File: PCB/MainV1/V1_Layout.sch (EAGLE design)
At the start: 50 parts, among them IC1 AD826N, IC3 AD623R, U2 MB85RC256VPF-G-JNERE2, X1 STEREOJACK

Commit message: Review changes complete. Starting layout
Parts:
- removed D7, D8: 1N4004, diode:1N4004
- C10: value (none) -> 10uF
- C11, C9: value (none) -> 1uF
- C7: value 1uF -> 10nF
- C8: value (none) -> 100nF
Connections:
- net AGND: no longer D7.C, D8.A
- net D6: no longer U2.A2
- net D7: no longer U2.A1
- net D8: no longer U2.A0
- net GND: now also U2.A0, U2.A1, U2.A2; no longer D7.A, D8.C
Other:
- note added: "Address: 0x1D and 0x1C"
- note added: "Address: 0x50"
- note added: "Address: 0x90"
- note removed: "Address changable from Arduino"
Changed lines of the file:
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@@
 <part name="SUPPLY15" library="supply2" library_urn="urn:adsk.eagle:library:372" deviceset="GND" device=""/>
 <part name="+3V10" library="supply1" library_urn="urn:adsk.eagle:library:371" deviceset="+3V3" device=""/>
-<part name="D7" library="diode" library_urn="urn:adsk.eagle:library:210" deviceset="1N4004" device="" package3d_urn="urn:adsk.eagle:package:43336/1"/>
-<part name="D8" library="diode" library_urn="urn:adsk.eagle:library:210" deviceset="1N4004" device="" package3d_urn="urn:adsk.eagle:package:43336/1"/>
-<part name="SUPPLY16" library="supply2" library_urn="urn:adsk.eagle:library:372" deviceset="GND" device=""/>
-<part name="AGND3" library="supply1" library_urn="urn:adsk.eagle:library:371" deviceset="AGND" device=""/>
 <part name="PWR" library="pinhead" library_urn="urn:adsk.eagle:library:325" deviceset="PINHD-1X2" device="" package3d_urn="urn:adsk.eagle:package:22435/2"/>
 <part name="R9" library="rcl" library_urn="urn:adsk.eagle:library:334" deviceset="R-US_" device="R0603" package3d_urn="urn:adsk.eagle:package:23555/2" value="10k"/>
@@
 <part name="SUPPLY20" library="supply2" library_urn="urn:adsk.eagle:library:372" deviceset="GND" device=""/>
 <part name="C6" library="rcl" library_urn="urn:adsk.eagle:library:334" deviceset="C-EU" device="C0603" package3d_urn="urn:adsk.eagle:package:23616/2" value="100nF"/>
-<part name="C7" library="rcl" library_urn="urn:adsk.eagle:library:334" deviceset="C-EU" device="C0603" package3d_urn="urn:adsk.eagle:package:23616/2" value="1uF"/>
-<part name="C8" library="rcl" library_urn="urn:adsk.eagle:library:334" deviceset="C-EU" device="025-030X050" package3d_urn="urn:adsk.eagle:package:23631/1"/>
-<part name="C9" library="rcl" library_urn="urn:adsk.eagle:library:334" deviceset="C-EU" device="025-030X050" package3d_urn="urn:adsk.eagle:package:23631/1"/>
-<part name="C10" library="rcl" library_urn="urn:adsk.eagle:library:334" deviceset="CPOL-EU" device="E3.5-8" package3d_urn="urn:adsk.eagle:package:23360/2"/>
-<part name="C11" library="rcl" library_urn="urn:adsk.eagle:library:334" deviceset="C-EU" device="025-030X050" package3d_urn="urn:adsk.eagle:package:23631/1"/>
+<part name="C7" library="rcl" library_urn="urn:adsk.eagle:library:334" deviceset="C-EU" device="C0603" package3d_urn="urn:adsk.eagle:package:23616/2" value="10nF"/>
+<part name="C8" library="rcl" library_urn="urn:adsk.eagle:library:334" deviceset="C-EU" device="025-030X050" package3d_urn="urn:adsk.eagle:package:23631/1" value="100nF"/>
+<part name="C9" library="rcl" library_urn="urn:adsk.eagle:library:334" deviceset="C-EU" device="025-030X050" package3d_urn="urn:adsk.eagle:package:23631/1" value="1uF"/>
+<part name="C10" library="rcl" library_urn="urn:adsk.eagle:library:334" deviceset="CPOL-EU" device="E3.5-8" package3d_urn="urn:adsk.eagle:package:23360/2" value="10uF"/>
+<part name="C11" library="rcl" library_urn="urn:adsk.eagle:library:334" deviceset="C-EU" device="025-030X050" package3d_urn="urn:adsk.eagle:package:23631/1" value="1uF"/>
 <part name="SUPPLY21" library="supply2" library_urn="urn:adsk.eagle:library:372" deviceset="GND" device=""/>
 <part name="+3V13" library="supply1" library_urn="urn:adsk.eagle:library:371" deviceset="+3V3" device=""/>
 <part name="SUPPLY22" library="supply2" library_urn="urn:adsk.eagle:library:372" deviceset="GND" device=""/>
+<part name="SUPPLY24" library="supply2" library_urn="urn:adsk.eagle:library:372" deviceset="GND" device=""/>
+<part name="AGND3" library="supply1" library_urn="urn:adsk.eagle:library:371" deviceset="AGND" device=""/>
 </parts>
 <sheets>
@@
 <wire x1="342.9" y1="55.88" x2="342.9" y2="116.84" width="0.254" layer="94"/>
 <text x="228.6" y="111.76" size="2.54" layer="94">EGC Signal Aplification</text>
-<text x="43.18" y="111.76" size="1.778" layer="97">Address changable from Arduino</text>
+<text x="43.18" y="111.76" size="1.778" layer="97">Address: 0x50</text>
 <wire x1="17.78" y1="55.88" x2="17.78" y2="-2.54" width="0.254" layer="94"/>
 <wire x1="17.78" y1="-2.54" x2="88.9" y2="-2.54" width="0.254" layer="94"/>
@@
 <wire x1="167.64" y1="-2.54" x2="88.9" y2="-2.54" width="0.254" layer="94"/>
 <text x="91.44" y="50.8" size="2.54" layer="94">Extra Bypass Capacitors</text>
+<text x="91.44" y="106.68" size="1.778" layer="97">Address: 0x1D and 0x1C</text>
+<text x="170.18" y="106.68" size="1.778" layer="97">Address: 0x90</text>
 </plain>
 <instances>
@@
 </instance>
 <instance part="AGND2" gate="VR1" x="292.1" y="71.12" smashed="yes">
-<attribute name="VALUE" x="289.56" y="66.04" size="1.778" layer="96" rot="R90"/>
+<attribute name="VALUE" x="299.72" y="73.66" size="1.778" layer="96" rot="R180"/>
 </instance>
 <instance part="+3V9" gate="G$1" x="287.02" y="109.22" smashed="yes">
@@
 <attribute name="VALUE" x="322.58" y="96.52" size="1.778" layer="96" rot="R90"/>
 </instance>
-<instance part="D7" gate="1" x="284.48" y="132.08" smashed="yes" rot="R90">
-<attribute name="NAME" x="283.9974" y="134.62" size="1.778" layer="95" rot="R90"/>
-<attribute name="VALUE" x="286.7914" y="137.16" size="1.778" layer="96" rot="R90"/>
-</instance>
-<instance part="D8" gate="1" x="289.56" y="132.08" smashed="yes" rot="R270">
-<attribute name="NAME" x="290.0426" y="129.54" size="1.778" layer="95" rot="R270"/>
-<attribute name="VALUE" x="289.7886" y="144.78" size="1.778" layer="96" rot="R270"/>
-</instance>
-<instance part="SUPPLY16" gate="GND" x="287.02" y="124.46" smashed="yes"/>
-<instance part="AGND3" gate="VR1" x="302.26" y="132.08" smashed="yes">
-<attribute name="VALUE" x="299.72" y="127" size="1.778" layer="96" rot="R90"/>
-</instance>
 <instance part="PWR" gate="G$1" x="99.06" y="190.5" smashed="yes" rot="R90">
 <attribute name="NAME" x="93.345" y="184.15" size="1.778" layer="95" rot="R90"/>
@@
 <instance part="SUPPLY22" gate="GND" x="129.54" y="12.7" smashed="yes">
 <attribute name="VALUE" x="127.635" y="9.525" size="1.778" layer="96"/>
+</instance>
+<instance part="SUPPLY24" gate="GND" x="35.56" y="68.58" smashed="yes"/>
+<instance part="AGND3" gate="VR1" x="302.26" y="132.08" smashed="yes">
+<attribute name="VALUE" x="299.72" y="127" size="1.778" layer="96" rot="R90"/>
 </instance>
 </instances>
@@
 <pinref part="SUPPLY15" gate="GND" pin="GND"/>
 <wire x1="325.12" y1="76.2" x2="325.12" y2="73.66" width="0.1524" layer="91"/>
-</segment>
-<segment>
-<pinref part="D7" gate="1" pin="A"/>
-<wire x1="284.48" y1="129.54" x2="284.48" y2="127" width="0.1524" layer="91"/>
-<pinref part="SUPPLY16" gate="GND" pin="GND"/>
-<wire x1="284.48" y1="127" x2="287.02" y2="127" width="0.1524" layer="91"/>
-<pinref part="D8" gate="1" pin="C"/>
-<wire x1="289.56" y1="129.54" x2="289.56" y2="127" width="0.1524" layer="91"/>
-<wire x1="289.56" y1="127" x2="287.02" y2="127" width="0.1524" layer="91"/>
-<junction x="287.02" y="127"/>
 </segment>
 <segment>
@@
 <junction x="139.7" y="20.32"/>
 </segment>
+<segment>
+<pinref part="U2" gate="G$1" pin="A2"/>
+<wire x1="45.72" y1="71.12" x2="35.56" y2="71.12" width="0.1524" layer="91"/>
+<pinref part="SUPPLY24" gate="GND" pin="GND"/>
+<pinref part="U2" gate="G$1" pin="A1"/>
+<wire x1="45.72" y1="73.66" x2="35.56" y2="73.66" width="0.1524" layer="91"/>
+<wire x1="35.56" y1="71.12" x2="35.56" y2="73.66" width="0.1524" layer="91"/>
+<junction x="35.56" y="71.12"/>
+<pinref part="U2" gate="G$1" pin="A0"/>
+<wire x1="45.72" y1="76.2" x2="35.56" y2="76.2" width="0.1524" layer="91"/>
+<wire x1="35.56" y1="73.66" x2="35.56" y2="76.2" width="0.1524" layer="91"/>
+<junction x="35.56" y="73.66"/>
+</segment>
 </net>
 <net name="N$2" class="0">
@@
 <pinref part="U$1" gate="G$1" pin="D8"/>
 <wire x1="43.18" y1="139.7" x2="33.02" y2="139.7" width="0.1524" layer="91"/>
-<label x="40.64" y="139.7" size="1.778" layer="95"/>
 <pinref part="JP1" gate="G$1" pin="2"/>
-</segment>
-<segment>
-<pinref part="U2" gate="G$1" pin="A0"/>
-<wire x1="45.72" y1="76.2" x2="35.56" y2="76.2" width="0.1524" layer="91"/>
-<label x="35.56" y="76.2" size="1.778" layer="95"/>
 </segment>
 </net>
@@
 <pinref part="U$1" gate="G$1" pin="D7"/>
 <wire x1="43.18" y1="142.24" x2="33.02" y2="142.24" width="0.1524" layer="91"/>
-<label x="40.64" y="142.24" size="1.778" layer="95"/>
 <pinref part="JP1" gate="G$1" pin="3"/>
-</segment>
-<segment>
-<pinref part="U2" gate="G$1" pin="A1"/>
-<wire x1="45.72" y1="73.66" x2="35.56" y2="73.66" width="0.1524" layer="91"/>
-<label x="35.56" y="73.66" size="1.778" layer="95"/>
 </segment>
 </net>
@@
 <pinref part="U$1" gate="G$1" pin="D6"/>
 <wire x1="43.18" y1="144.78" x2="33.02" y2="144.78" width="0.1524" layer="91"/>
-<label x="40.64" y="144.78" size="1.778" layer="95"/>
 <pinref part="JP1" gate="G$1" pin="4"/>
-</segment>
-<segment>
-<pinref part="U2" gate="G$1" pin="A2"/>
-<wire x1="45.72" y1="71.12" x2="35.56" y2="71.12" width="0.1524" layer="91"/>
-<label x="35.56" y="71.12" size="1.778" layer="95"/>
 </segment>
 </net>
@@
 <segment>
 <pinref part="R3" gate="G$1" pin="2"/>
-<wire x1="281.94" y1="137.16" x2="284.48" y2="137.16" width="0.1524" layer="91"/>
-<pinref part="D7" gate="1" pin="C"/>
-<wire x1="284.48" y1="137.16" x2="284.48" y2="134.62" width="0.1524" layer="91"/>
-<pinref part="D8" gate="1" pin="A"/>
-<wire x1="284.48" y1="137.16" x2="289.56" y2="137.16" width="0.1524" layer="91"/>
-<wire x1="289.56" y1="137.16" x2="289.56" y2="134.62" width="0.1524" layer="91"/>
-<junction x="284.48" y="137.16"/>
-<wire x1="289.56" y1="137.16" x2="302.26" y2="137.16" width="0.1524" layer="91"/>
-<junction x="289.56" y="137.16"/>
+<wire x1="281.94" y1="137.16" x2="302.26" y2="137.16" width="0.1524" layer="91"/>
 <wire x1="302.26" y1="137.16" x2="302.26" y2="134.62" width="0.1524" layer="91"/>
 <pinref part="AGND3" gate="VR1" pin="AGND"/>

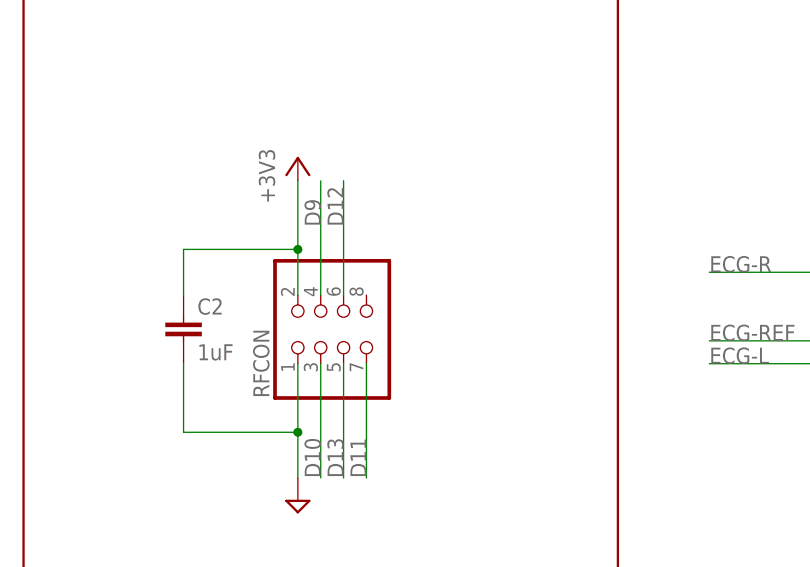
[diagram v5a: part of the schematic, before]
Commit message: Finished routing Temp Buddy Board. Please review.
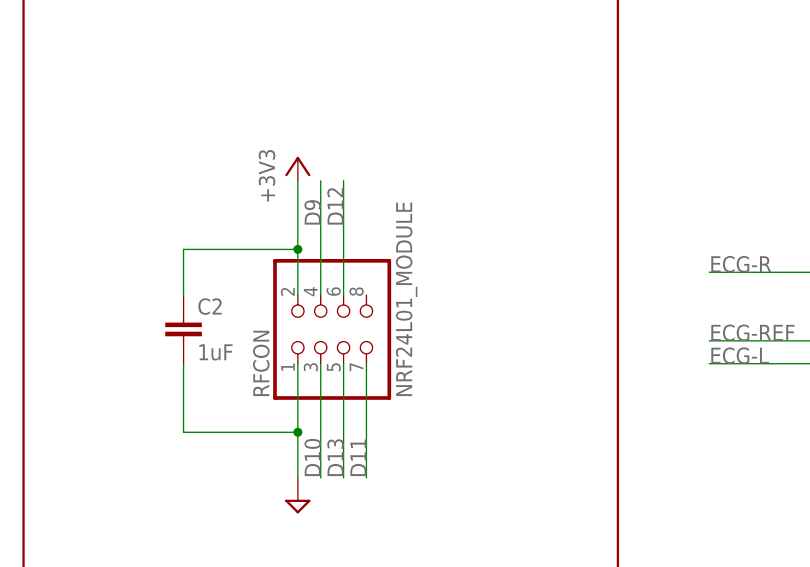
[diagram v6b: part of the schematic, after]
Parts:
- RFCON: value (none) -> NRF24L01_MODULE; device pinhead:PINHD-2X4 -> Custom Parts:NRF24L01_MODULE
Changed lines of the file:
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@@
 </variantdefs>
 <classes>
-<class number="0" name="default" width="0" drill="0">
+<class number="0" name="default" width="0.4064" drill="0">
+</class>
+<class number="1" name="POWER" width="0.8128" drill="0">
 </class>
 </classes>
@@
 <part name="SUPPLY7" library="supply2" library_urn="urn:adsk.eagle:library:372" deviceset="GND" device=""/>
 <part name="+3V2" library="supply1" library_urn="urn:adsk.eagle:library:371" deviceset="+3V3" device=""/>
-<part name="RFCON" library="pinhead" library_urn="urn:adsk.eagle:library:325" deviceset="PINHD-2X4" device="" package3d_urn="urn:adsk.eagle:package:22461/2"/>
 <part name="SUPPLY10" library="supply2" library_urn="urn:adsk.eagle:library:372" deviceset="GND" device=""/>
 <part name="+3V3" library="supply1" library_urn="urn:adsk.eagle:library:371" deviceset="+3V3" device=""/>
@@
 <part name="SUPPLY24" library="supply2" library_urn="urn:adsk.eagle:library:372" deviceset="GND" device=""/>
 <part name="AGND3" library="supply1" library_urn="urn:adsk.eagle:library:371" deviceset="AGND" device=""/>
+<part name="RFCON" library="Custom Parts" deviceset="NRF24L01_MODULE" device=""/>
 </parts>
 <sheets>
@@
 <attribute name="VALUE" x="71.12" y="86.36" size="1.778" layer="96" rot="R90"/>
 </instance>
-<instance part="RFCON" gate="A" x="144.78" y="157.48" smashed="yes" rot="R90">
-<attribute name="NAME" x="136.525" y="151.13" size="1.778" layer="95" rot="R90"/>
-<attribute name="VALUE" x="152.4" y="151.13" size="1.778" layer="96" rot="R90"/>
-</instance>
 <instance part="SUPPLY10" gate="GND" x="139.7" y="139.7" smashed="yes"/>
 <instance part="+3V3" gate="G$1" x="139.7" y="177.8" smashed="yes">
@@
 <instance part="AGND3" gate="VR1" x="302.26" y="132.08" smashed="yes">
 <attribute name="VALUE" x="299.72" y="127" size="1.778" layer="96" rot="R90"/>
+</instance>
+<instance part="RFCON" gate="G$1" x="144.78" y="157.48" smashed="yes" rot="R90">
+<attribute name="NAME" x="136.525" y="151.13" size="1.778" layer="95" rot="R90"/>
+<attribute name="VALUE" x="152.4" y="151.13" size="1.778" layer="96" rot="R90"/>
 </instance>
 </instances>
@@
 </segment>
 <segment>
-<pinref part="RFCON" gate="A" pin="1"/>
 <wire x1="139.7" y1="154.94" x2="139.7" y2="147.32" width="0.1524" layer="91"/>
 <pinref part="SUPPLY10" gate="GND" pin="GND"/>
@@
 <wire x1="127" y1="147.32" x2="139.7" y2="147.32" width="0.1524" layer="91"/>
 <junction x="139.7" y="147.32"/>
+<pinref part="RFCON" gate="G$1" pin="1"/>
 </segment>
 <segment>
@@
 </segment>
 </net>
-<net name="+3V3" class="0">
+<net name="+3V3" class="1">
 <segment>
 <pinref part="U2" gate="G$1" pin="VCC"/>
@@
 </segment>
 <segment>
-<pinref part="RFCON" gate="A" pin="2"/>
 <wire x1="139.7" y1="162.56" x2="139.7" y2="167.64" width="0.1524" layer="91"/>
 <pinref part="+3V3" gate="G$1" pin="+3V3"/>
@@
 <wire x1="127" y1="167.64" x2="139.7" y2="167.64" width="0.1524" layer="91"/>
 <junction x="139.7" y="167.64"/>
+<pinref part="RFCON" gate="G$1" pin="2"/>
 </segment>
 <segment>
@@
 <net name="D10" class="0">
 <segment>
-<pinref part="RFCON" gate="A" pin="3"/>
 <wire x1="142.24" y1="154.94" x2="142.24" y2="142.24" width="0.1524" layer="91"/>
 <label x="142.24" y="142.24" size="1.778" layer="95" rot="R90"/>
+<pinref part="RFCON" gate="G$1" pin="3"/>
 </segment>
 <segment>
@@
 <net name="D13" class="0">
 <segment>
-<pinref part="RFCON" gate="A" pin="5"/>
 <wire x1="144.78" y1="154.94" x2="144.78" y2="142.24" width="0.1524" layer="91"/>
 <label x="144.78" y="142.24" size="1.778" layer="95" rot="R90"/>
+<pinref part="RFCON" gate="G$1" pin="5"/>
 </segment>
 <segment>
@@
 <net name="D11" class="0">
 <segment>
-<pinref part="RFCON" gate="A" pin="7"/>
 <wire x1="147.32" y1="154.94" x2="147.32" y2="142.24" width="0.1524" layer="91"/>
 <label x="147.32" y="142.24" size="1.778" layer="95" rot="R90"/>
+<pinref part="RFCON" gate="G$1" pin="7"/>
 </segment>
 <segment>
@@
 <net name="D9" class="0">
 <segment>
-<pinref part="RFCON" gate="A" pin="4"/>
 <wire x1="142.24" y1="162.56" x2="142.24" y2="175.26" width="0.1524" layer="91"/>
 <label x="142.24" y="170.18" size="1.778" layer="95" rot="R90"/>
+<pinref part="RFCON" gate="G$1" pin="4"/>
 </segment>
 <segment>
@@
 <net name="D12" class="0">
 <segment>
-<pinref part="RFCON" gate="A" pin="6"/>
 <wire x1="144.78" y1="162.56" x2="144.78" y2="175.26" width="0.1524" layer="91"/>
 <label x="144.78" y="170.18" size="1.778" layer="95" rot="R90"/>
-</segment>
-<segment>
+<pinref part="RFCON" gate="G$1" pin="6"/>
+</segment>
+<segment>
